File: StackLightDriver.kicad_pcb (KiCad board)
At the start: 4 copper layers, 100 x 100 mm, 99 parts, among them J1 B2B-XH-A, J10 B2B-XH-A, J11 PJ-102AH, J12 USB_C_Receptacle_USB2.0_14P, J2 B2B-XH-A, J3 B2B-XH-A, J4 B2B-XH-A, J5 B2B-XH-A, J6 B2B-XH-A, J7 B2B-XH-A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

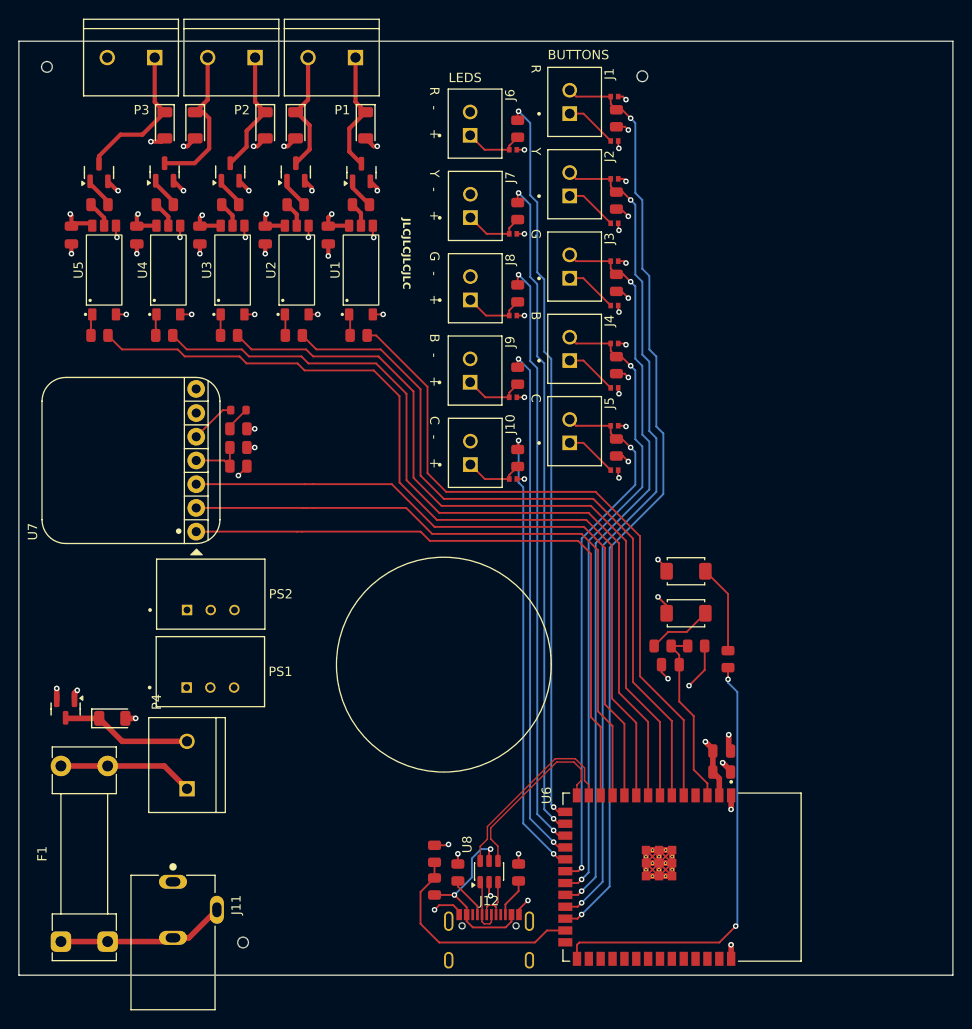
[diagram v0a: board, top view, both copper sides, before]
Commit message: DRC adjustments
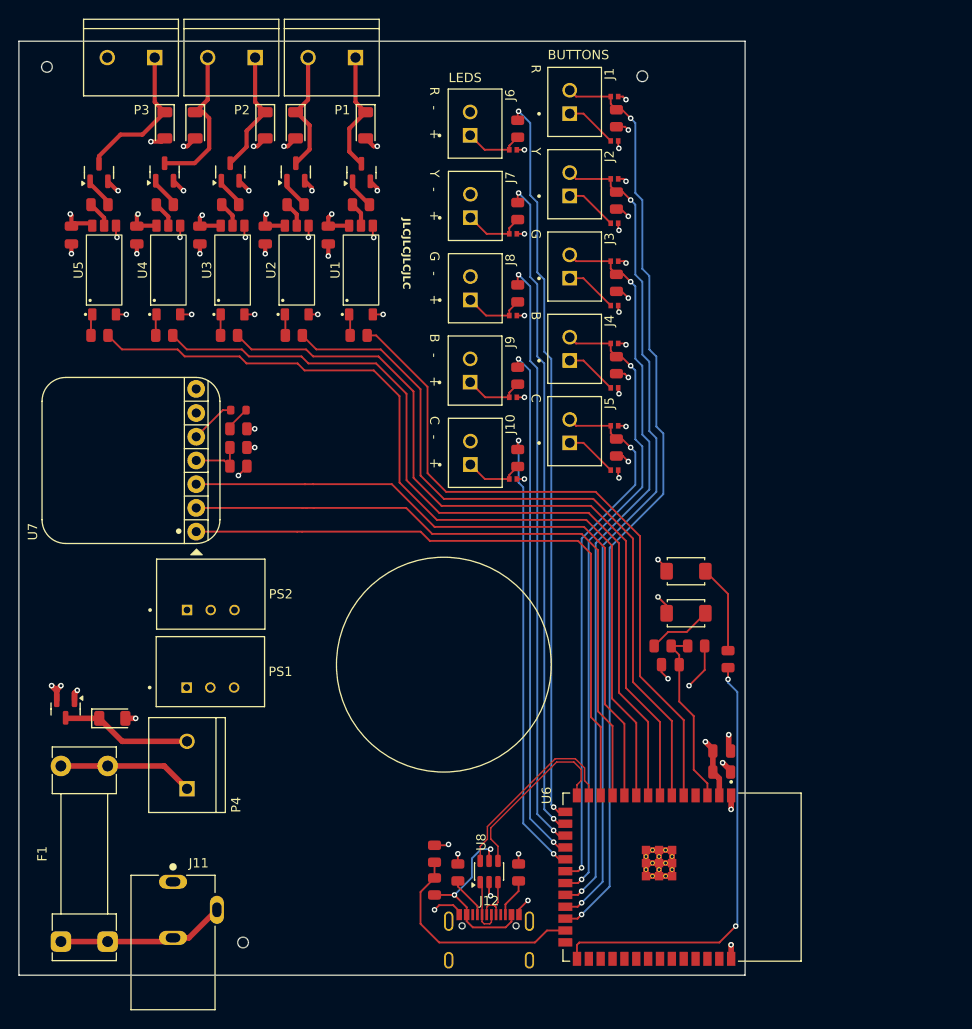
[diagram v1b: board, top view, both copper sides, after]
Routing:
- net GND: track 104.3 -> 88.4 mm
- net VSupply: track 26.4 -> 27.6 mm, vias 11 -> 12
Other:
- board size 100 x 100 mm -> 77.8 x 100 mm
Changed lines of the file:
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@@
 		(pad "41_10" thru_hole circle
 			(at -1.5 1.76 270)
-			(size 0.4 0.4)
-			(drill 0.2)
+			(size 0.5 0.5)
+			(drill 0.3)
 			(layers "*.Cu")
 			(remove_unused_layers no)
@@
 		(pad "41_11" thru_hole circle
 			(at -2.9 1.76 270)
-			(size 0.4 0.4)
-			(drill 0.2)
+			(size 0.5 0.5)
+			(drill 0.3)
 			(layers "*.Cu")
 			(remove_unused_layers no)
@@
 		(pad "41_12" thru_hole circle
 			(at -0.1 1.76 270)
-			(size 0.4 0.4)
-			(drill 0.2)
+			(size 0.5 0.5)
+			(drill 0.3)
 			(layers "*.Cu")
 			(remove_unused_layers no)
@@
 		(pad "41_13" thru_hole circle
 			(at -2.9 3.16 270)
-			(size 0.4 0.4)
-			(drill 0.2)
+			(size 0.5 0.5)
+			(drill 0.3)
 			(layers "*.Cu")
 			(remove_unused_layers no)
@@
 		(pad "41_14" thru_hole circle
 			(at -1.5 3.16 270)
-			(size 0.4 0.4)
-			(drill 0.2)
+			(size 0.5 0.5)
+			(drill 0.3)
 			(layers "*.Cu")
 			(remove_unused_layers no)
@@
 		(pad "41_15" thru_hole circle
 			(at -0.1 3.16 270)
-			(size 0.4 0.4)
-			(drill 0.2)
+			(size 0.5 0.5)
+			(drill 0.3)
 			(layers "*.Cu")
 			(remove_unused_layers no)
@@
 		(pad "41_16" thru_hole circle
 			(at -2.2 1.06 270)
-			(size 0.4 0.4)
-			(drill 0.2)
+			(size 0.5 0.5)
+			(drill 0.3)
 			(layers "*.Cu")
 			(remove_unused_layers no)
@@
 		(pad "41_17" thru_hole circle
 			(at -0.8 1.06 270)
-			(size 0.4 0.4)
-			(drill 0.2)
+			(size 0.5 0.5)
+			(drill 0.3)
 			(layers "*.Cu")
 			(remove_unused_layers no)
@@
 		(pad "41_18" thru_hole circle
 			(at -2.2 2.46 270)
-			(size 0.4 0.4)
-			(drill 0.2)
+			(size 0.5 0.5)
+			(drill 0.3)
 			(layers "*.Cu")
 			(remove_unused_layers no)
@@
 		(pad "41_19" thru_hole circle
 			(at -0.8 2.46 270)
-			(size 0.4 0.4)
-			(drill 0.2)
+			(size 0.5 0.5)
+			(drill 0.3)
 			(layers "*.Cu")
 			(remove_unused_layers no)
@@
 		(pad "41_20" thru_hole circle
 			(at -2.2 3.86 270)
-			(size 0.4 0.4)
-			(drill 0.2)
+			(size 0.5 0.5)
+			(drill 0.3)
 			(layers "*.Cu")
 			(remove_unused_layers no)
@@
 		(pad "41_21" thru_hole circle
 			(at -0.8 3.86 270)
-			(size 0.4 0.4)
-			(drill 0.2)
+			(size 0.5 0.5)
+			(drill 0.3)
 			(layers "*.Cu")
 			(remove_unused_layers no)
@@
 			(net 0)
 			(net_name "")
-			(layers "F.Cu" "B.Cu")
+			(layers "F.Cu" "B.Cu" "In1.Cu" "In2.Cu")
 			(hatch full 0.508)
 			(connect_pads
@@
 		(at 77 111.5 90)
 		(property "Reference" "P4"
-			(at 6.75 -3.25 90)
+			(at -4.25 5.25 90)
 			(layer "F.SilkS")
 			(effects
@@
 		(tags "SOT TO_SOT_SMD")
 		(property "Reference" "U8"
-			(at 2.9 -2.34 90)
+			(at 3.15 -0.84 90)
 			(layer "F.SilkS")
 			(effects
@@
 		(at 75.5 130.5 -90)
 		(property "Reference" "J11"
-			(at -4.01986 -6.77319 90)
+			(at -8.5 -2.75 0)
 			(layer "F.SilkS")
 			(effects
@@
 			(size 1 1)
 			(drill 1.152)
-			(layers "*.Cu" "*.Mask")
+			(layers "F&B.Cu" "*.Mask")
 			(solder_mask_margin 0.148)
 			(teardrops
@@
 			(net 0)
 			(net_name "")
-			(layers "F.Cu" "B.Cu" "F.SilkS" "B.SilkS" "F.Paste" "B.Paste" "B.CrtYd"
-				"F.CrtYd"
+			(layers "F.Cu" "B.Cu" "In1.Cu" "F.SilkS" "In2.Cu" "B.SilkS" "F.Paste"
+				"B.Paste" "B.CrtYd" "F.CrtYd"
 			)
 			(hatch edge 0.5)
@@
 	(gr_rect
 		(start 59 34)
-		(end 159 134)
+		(end 136.75 134)
 		(stroke
 			(width 0.05)
@@
 	)
 	(segment
-		(start 127.54 123.4)
-		(end 126.14 122)
-		(width 0.2)
-		(layer "F.Cu")
-		(net 1)
-	)
-	(segment
 		(start 126.14 121.3)
 		(end 126.14 122)
@@
 	)
 	(segment
-		(start 127.54 122)
-		(end 128.94 120.6)
-		(width 0.2)
-		(layer "F.Cu")
-		(net 1)
-	)
-	(segment
-		(start 127.54 120.6)
-		(end 128.94 122)
-		(width 0.2)
-		(layer "F.Cu")
-		(net 1)
-	)
-	(segment
 		(start 128.94 123.4)
 		(end 128.94 122.7)
@@
 	)
 	(segment
-		(start 127.54 122)
-		(end 126.14 123.4)
-		(width 0.2)
-		(layer "F.Cu")
-		(net 1)
-	)
-	(segment
 		(start 69.395 63.25)
 		(end 70.5 63.25)
@@
 	)
 	(segment
-		(start 126.14 120.6)
-		(end 127.54 122)
-		(width 0.2)
-		(layer "F.Cu")
-		(net 1)
-	)
-	(segment
 		(start 128.35 94.425)
 		(end 127.425 93.5)
@@
 	(segment
 		(start 128.94 122)
-		(end 127.54 123.4)
-		(width 0.2)
-		(layer "F.Cu")
-		(net 1)
-	)
-	(segment
-		(start 128.94 122)
 		(end 128.94 121.3)
 		(width 0.6)
@@
 	)
 	(segment
-		(start 127.54 120.6)
-		(end 126.14 122)
-		(width 0.2)
-		(layer "F.Cu")
-		(net 1)
-	)
-	(segment
 		(start 113.12675 45.62325)
 		(end 112.306 45.62325)
@@
 	)
 	(segment
-		(start 127.54 122)
-		(end 128.94 123.4)
-		(width 0.2)
-		(layer "F.Cu")
-		(net 1)
-	)
-	(segment
 		(start 83.145 53.75)
 		(end 83.145 54.895)
@@
 	)
 	(segment
-		(start 63.05 104.56)
-		(end 63.05 103.3)
-		(width 0.6)
-		(layer "F.Cu")
-		(net 2)
-	)
-	(segment
 		(start 69.525 50)
 		(end 69.625 50)
@@
 	)
 	(segment
+		(start 63.05 103.55)
+		(end 62.5 103)
+		(width 0.6)
+		(layer "F.Cu")
+		(net 2)
+	)
+	(segment
 		(start 85.425 53.75)
 		(end 85.375 53.8)
@@
 	)
 	(segment
+		(start 63.05 103.55)
+		(end 63.05 103.45)
+		(width 0.6)
+		(layer "F.Cu")
+		(net 2)
+	)
+	(segment
+		(start 63.05 103.45)
+		(end 63.5 103)
+		(width 0.6)
+		(layer "F.Cu")
+		(net 2)
+	)
+	(segment
 		(start 87.48 53.75)
 		(end 85.425 53.75)
@@
 	)
 	(segment
+		(start 63.05 104.56)
+		(end 63.05 103.55)
+		(width 0.6)
+		(layer "F.Cu")
+		(net 2)
+	)
+	(segment
 		(start 64.925 53.5)
 		(end 64.625 53.8)
@@
 	)
 	(via
-		(at 63.05 103.3)
+		(at 62.5 103)
+		(size 0.6)
+		(drill 0.3)
+		(layers "F.Cu" "B.Cu")
+		(net 2)
+	)
+	(via
+		(at 63.5 103)
 		(size 0.6)
 		(drill 0.3)
@@
 	)
 	(segment
-		(start 75.1 130.4)
-		(end 75.5 130)
-		(width 0.6)
-		(layer "F.Cu")
-		(net 76)
-	)
-	(segment
 		(start 77.2 130)
 		(end 80.2 127)
@@
 	)
 	(segment
-		(start 68.5 130.4)
-		(end 75.1 130.4)
+		(start 75.1 130.4)
+		(end 75.5 130)
 		(width 0.6)
 		(layer "F.Cu")
@@
 		(width 0.6)
 		(layer "F.Cu")
+		(net 76)
+	)
+	(segment
+		(start 68.5 130.4)
+		(end 75.1 130.4)
+		(width 0.6)
+		(layer "F.Cu")

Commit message: Mounting and tooling holes, silkscreen work
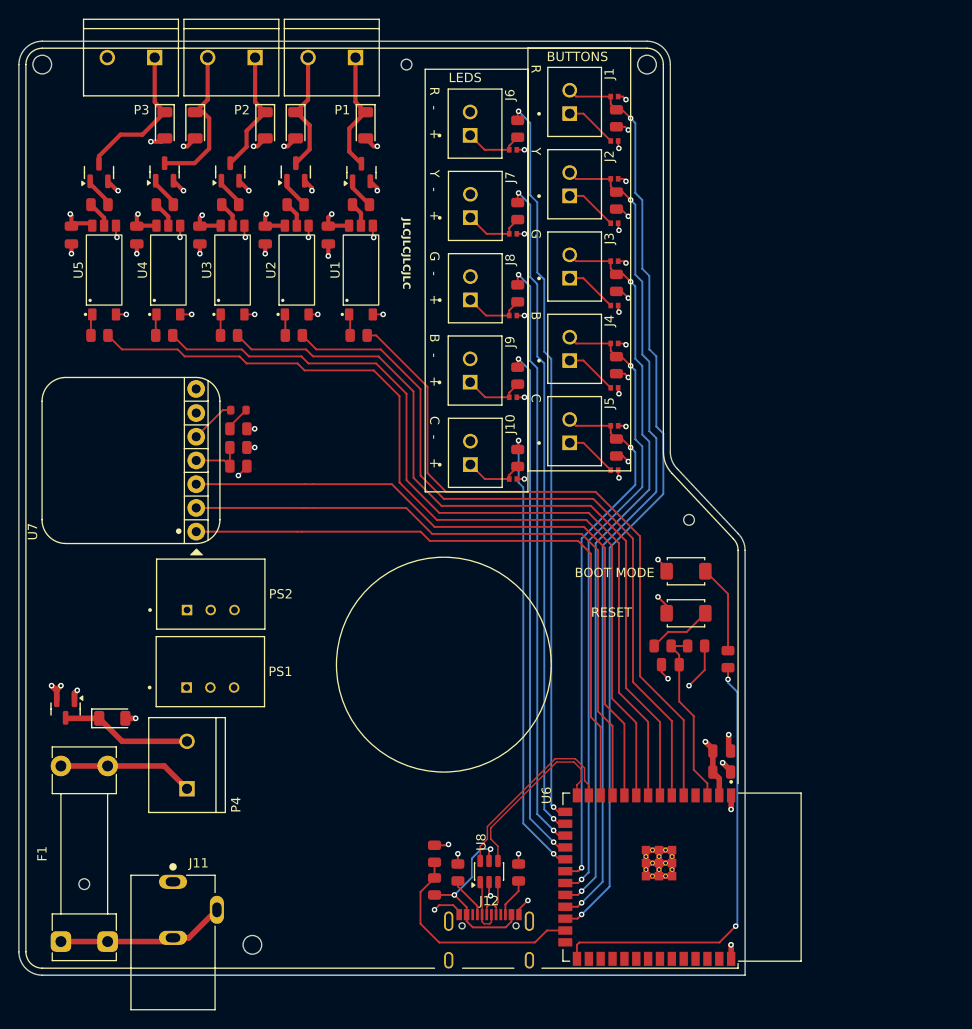
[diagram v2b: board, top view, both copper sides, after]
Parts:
- removed H1, H2, H3: ~, PCM_JLCPCB:Hole_Tooling_JLCPCB
- added ?: , , F.Cu at (84.0, 130.8)
- added ?: , , F.Cu at (61.5, 36.5)
- added REF**: Tooling_hole, Project_footprints:Tooling_hole, F.Cu at (66.0, 124.2)
- added REF**: Tooling_hole, Project_footprints:Tooling_hole, F.Cu at (130.8, 85.2)
- added REF**: Tooling_hole, Project_footprints:Tooling_hole, F.Cu at (100.5, 36.5)
- added REF**: Mounting Hole, Project_footprints:Mounting Hole, F.Cu at (126.2, 36.5)
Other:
- outline, holes or cut-outs redrawn
- board text added: "BLUE"
- board text added: "BOOT MODE"
- board text added: "GND"
- board text added: "GREEN"
- board text added: "RED"
- board text added: "RESET"
- board text added: "USB-C 2.0"
- board text added: "WHITE"
- board text added: "YELLOW"

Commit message: Changed terminal block footprint, silkscreen changes, holes for speaker
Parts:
- removed P2, P3: 282837-2, Project_footprints:TE_282837-2
- added REF**: Tooling_hole, Project_footprints:Tooling_hole, F.Cu at (101.0, 115.0)
- added REF**: Tooling_hole, Project_footprints:Tooling_hole, F.Cu at (101.0, 87.8)
- P1: value 282837-2 -> 282837-2-6; footprint Project_footprints:TE_282837-2 -> Project_footprints:TE_282837-2-6
- moved P1 0.09 mm to (92.4, 35.8)
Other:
- board text added: "13.5V DC 2A"
- board text added: "2A"
- board text added: "4Ω 5W"
- board text added: "W"
- board text removed: "Switch goes here"

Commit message: Silly silk screen stuff, re-verified ESP32 pins
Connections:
- U6 pad 16: /BUTTON_LED_YELLOW -> unconnected-(U6-IO46-Pad16)
- U6 pad 17: /BUTTON_LED_GREEN -> /BUTTON_LED_YELLOW
- U6 pad 18: /BUTTON_LED_BLUE -> /BUTTON_LED_GREEN
- U6 pad 19: /BUTTON_LED_WHITE -> /BUTTON_LED_BLUE
- U6 pad 20: /BUTTON_WHITE -> /BUTTON_LED_WHITE
- U6 pad 21: /BUTTON_BLUE -> /BUTTON_WHITE
- U6 pad 22: /BUTTON_GREEN -> /BUTTON_BLUE
- U6 pad 23: /BUTTON_YELLOW -> /BUTTON_GREEN
- U6 pad 24: /BUTTON_RED -> /BUTTON_YELLOW
- U6 pad 25: /USB_POWER_IN_SIGNAL -> /BUTTON_RED
- U6 pad 31: unconnected-(U6-IO38-Pad31) -> /USB_POWER_IN_SIGNAL
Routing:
- net /USB_POWER_IN_SIGNAL: track 24.1 -> 31.4 mm, vias 0 -> 2
- net /BUTTON_GREEN: track 79.2 -> 80.4 mm
- net /BUTTON_LED_YELLOW: track 71.1 -> 72.3 mm
- net /BUTTON_WHITE: track 57.7 -> 59.0 mm
- net /BUTTON_LED_GREEN: track 63.7 -> 64.9 mm
- net /BUTTON_YELLOW: track 89.9 -> 91.1 mm
- net /BUTTON_RED: track 100.5 -> 101.8 mm
- net /BUTTON_LED_WHITE: track 48.3 -> 49.6 mm
- net /BUTTON_LED_BLUE: track 55.6 -> 56.8 mm
- net /BUTTON_BLUE: track 68.4 -> 69.6 mm
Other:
- board text added: "Stack Light Controller V1"

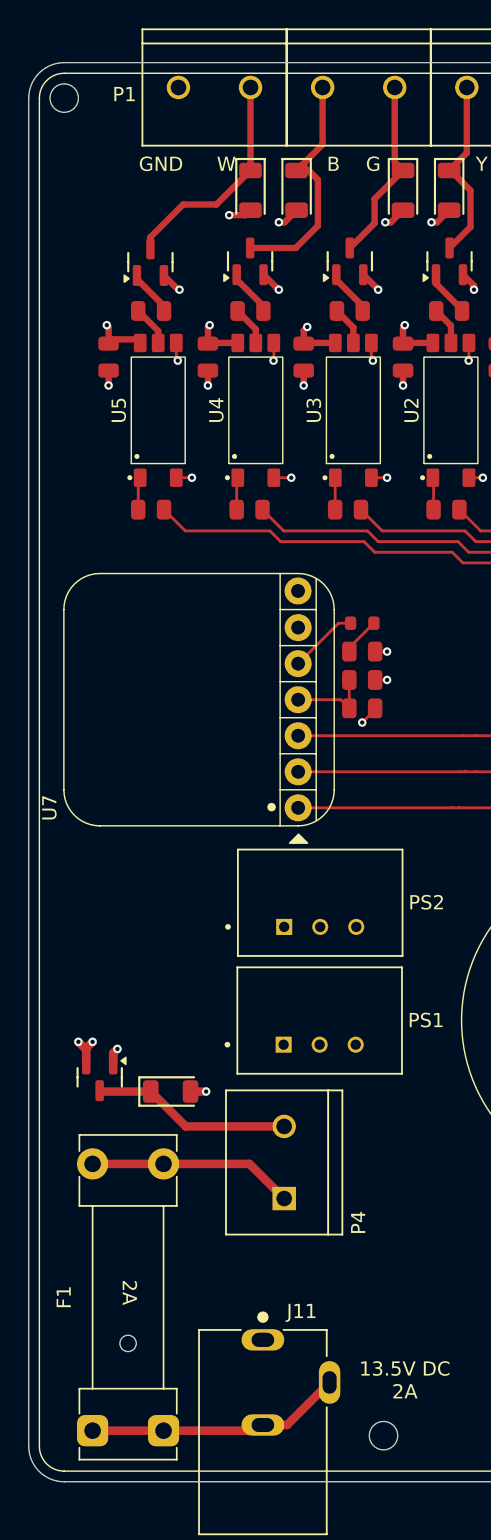
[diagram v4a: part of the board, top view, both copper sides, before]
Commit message: Terminal block courtyard, mounting/tooling hole references
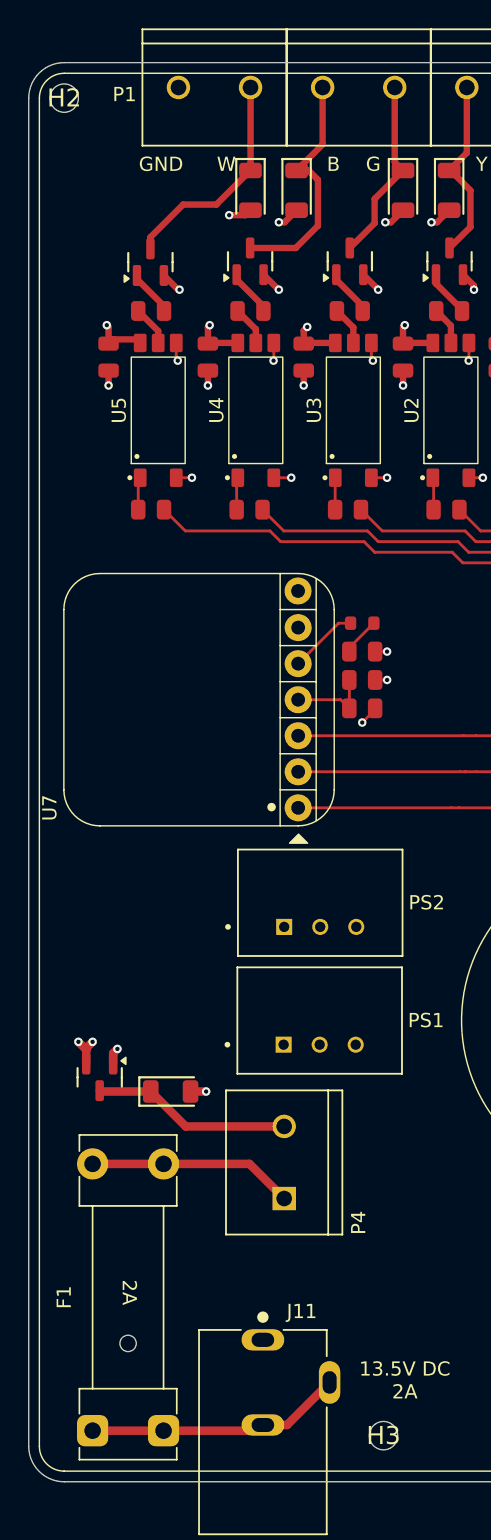
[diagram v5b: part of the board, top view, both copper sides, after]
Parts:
- H1: renamed from REF**; value Mounting Hole -> Mounting_hole; footprint Project_footprints:Mounting Hole -> Project_footprints:Mounting_hole
- H2: renamed from ?; value (none) -> Mounting Hole
- H3: renamed from ?; value (none) -> Mounting hole
- renumbered REF** to H4, REF** to H5, REF** to H6, REF** to H7, REF** to H8
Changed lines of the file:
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@@
 		(layer "F.Cu")
 		(at 66 124.25)
-		(property "Reference" "REF**"
+		(property "Reference" "H4"
 			(at 0 -0.5 0)
 			(unlocked yes)
@@
 		(layer "F.Cu")
 		(at 130.75 85.25)
-		(property "Reference" "REF**"
+		(property "Reference" "H6"
 			(at 0 -0.5 0)
 			(unlocked yes)
@@
 		(layer "F.Cu")
 		(at 101 115)
-		(property "Reference" "REF**"
+		(property "Reference" "H8"
 			(at 0 -0.5 0)
 			(unlocked yes)
@@
 		(layer "F.Cu")
 		(at 101 87.75)
-		(property "Reference" "REF**"
+		(property "Reference" "H7"
 			(at 0 -0.5 0)
 			(unlocked yes)
@@
 		(layer "F.Cu")
 		(at 100.5 36.5)
-		(property "Reference" "REF**"
+		(property "Reference" "H5"
 			(at 0 -0.5 0)
 			(unlocked yes)
@@
 			(layer "F.SilkS")
 		)
-		(fp_line
-			(start 25.65 -4.35)
-			(end 25.65 4.35)
-			(stroke
-				(width 0.05)
-				(type solid)
-			)
-			(layer "F.CrtYd")
-		)
-		(fp_line
-			(start 15.24 4.35)
-			(end 25.65 4.35)
-			(stroke
-				(width 0.05)
-				(type solid)
-			)
-			(layer "F.CrtYd")
-		)
-		(fp_line
-			(start 14.99 -4.35)
-			(end 25.65 -4.35)
-			(stroke
-				(width 0.05)
-				(type solid)
-			)
-			(layer "F.CrtYd")
-		)
-		(fp_line
-			(start 5.33 4.35)
-			(end -5.33 4.35)
-			(stroke
-				(width 0.05)
-				(type solid)
-			)
-			(layer "F.CrtYd")
-		)
-		(fp_line
-			(start 5.08 4.35)
-			(end 15.74 4.35)
-			(stroke
-				(width 0.05)
-				(type solid)
-			)
-			(layer "F.CrtYd")
-		)
-		(fp_line
-			(start 4.83 -4.35)
-			(end 15.49 -4.35)
-			(stroke
-				(width 0.05)
-				(type solid)
-			)
-			(layer "F.CrtYd")
-		)
-		(fp_line
-			(start -5.33 4.35)
-			(end -5.33 -4.35)
-			(stroke
-				(width 0.05)
-				(type solid)
-			)
-			(layer "F.CrtYd")
-		)
-		(fp_line
+		(fp_rect
 			(start -5.33 -4.35)
-			(end 5.33 -4.35)
+			(end 25.65 4.35)
 			(stroke
 				(width 0.05)
-				(type solid)
+				(type default)
 			)
+			(fill no)
 			(layer "F.CrtYd")
 		)
@@
 		(layer "F.Cu")
 		(at 84 130.75)
-		(property "Reference" ""
+		(property "Reference" "H3"
 			(at 0 0 0)
 			(layer "F.SilkS")
@@
 			)
 		)
-		(property "Value" ""
+		(property "Value" "Mounting hole"
 			(at 0 0 0)
 			(layer "F.Fab")
@@
 		)
 	)
-	(footprint "Project_footprints:Mounting Hole"
+	(footprint "Project_footprints:Mounting_hole"
 		(layer "F.Cu")
 		(at 126.25 36.5)
-		(property "Reference" "REF**"
+		(property "Reference" "H1"
 			(at 0 -0.5 0)
 			(unlocked yes)
@@
 			)
 		)
-		(property "Value" "Mounting Hole"
+		(property "Value" "Mounting_hole"
 			(at 0 1 0)
 			(unlocked yes)
@@
 		(layer "F.Cu")
 		(at 61.5 36.5)
-		(property "Reference" ""
+		(property "Reference" "H2"
 			(at 0 0 0)
 			(layer "F.SilkS")
@@
 			)
 		)
-		(property "Value" ""
+		(property "Value" "Mounting Hole"
 			(at 0 0 0)
 			(layer "F.Fab")
